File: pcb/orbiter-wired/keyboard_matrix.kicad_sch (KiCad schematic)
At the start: 89 parts, among them SW10 SW_Push, SW11 SW_Push, SW12 SW_Push, SW13 SW_Push, SW14 SW_Push, SW15 SW_Push, SW16 SW_Push, SW17 SW_Push, SW18 SW_Push, SW19 SW_Push, SW2 SW_Push, SW20 SW_Push, SW21 SW_Push, SW22 SW_Push, SW23 SW_Push, SW24 SW_Push, SW25 SW_Push, SW26 SW_Push, SW27 SW_Push, SW3 SW_Push, SW4 SW_Push, SW5 SW_Push, SW6 SW_Push, SW7 SW_Push, SW8 SW_Push, SW9 SW_Push

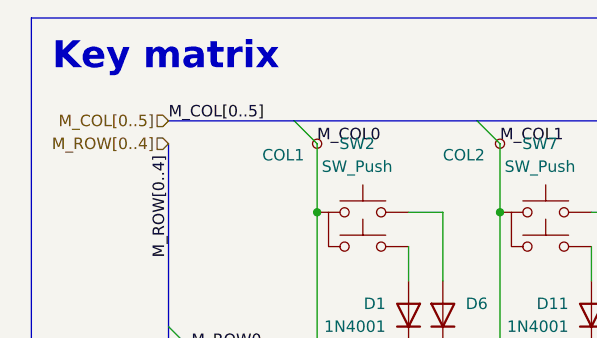
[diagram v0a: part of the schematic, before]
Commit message: Bump to Kicad 9
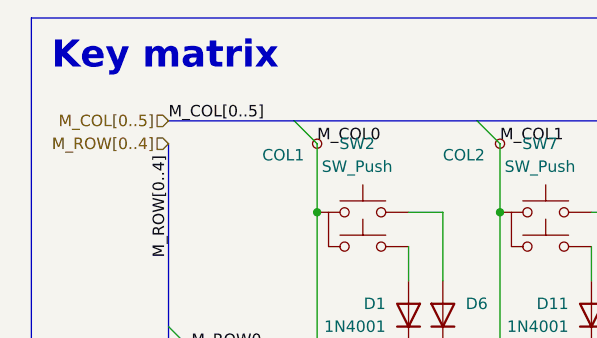
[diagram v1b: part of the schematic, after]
